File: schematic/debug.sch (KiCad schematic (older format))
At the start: 20 parts, among them J301 DEBUG HEADER, J302 DEBUG HEADER, U301 ATF16V8C_DEBUG, U302 ATF16V8C_DEBUG

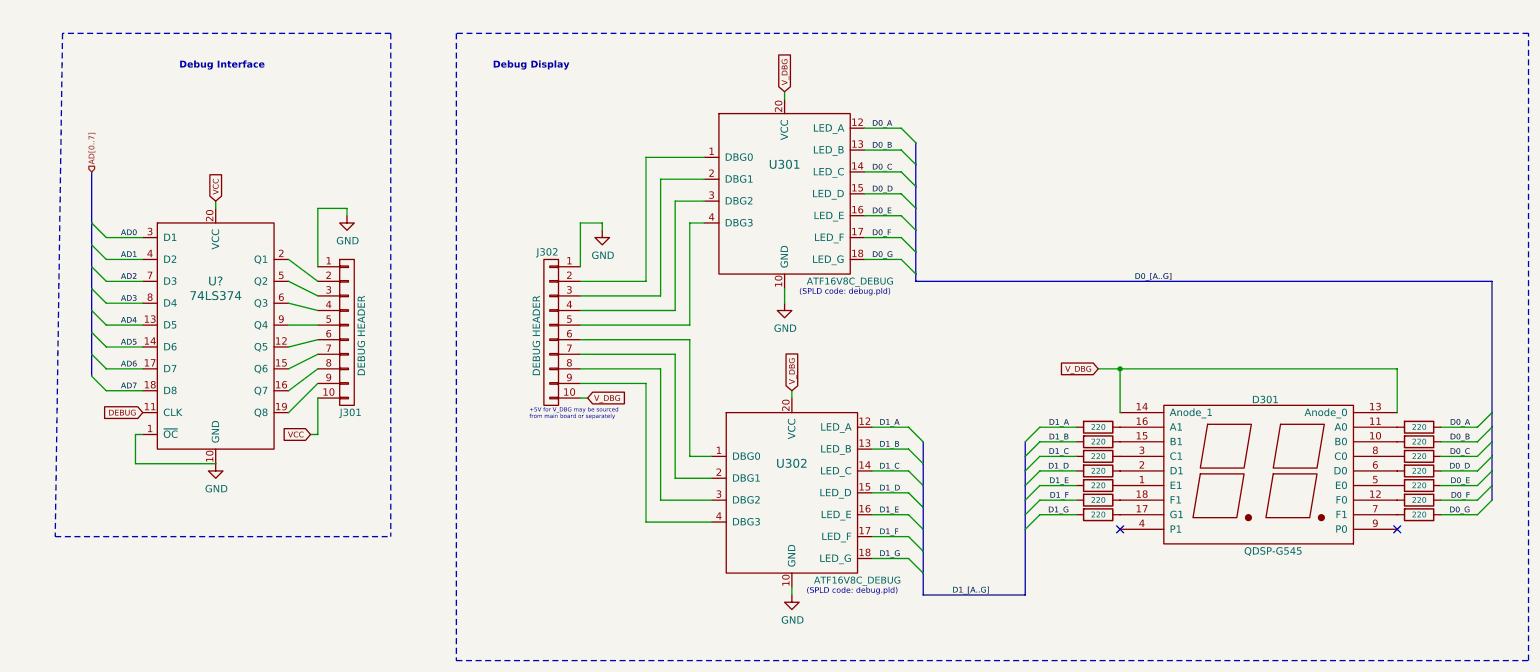
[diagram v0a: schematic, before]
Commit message: [L3] Update schematic with new NVRAM signals
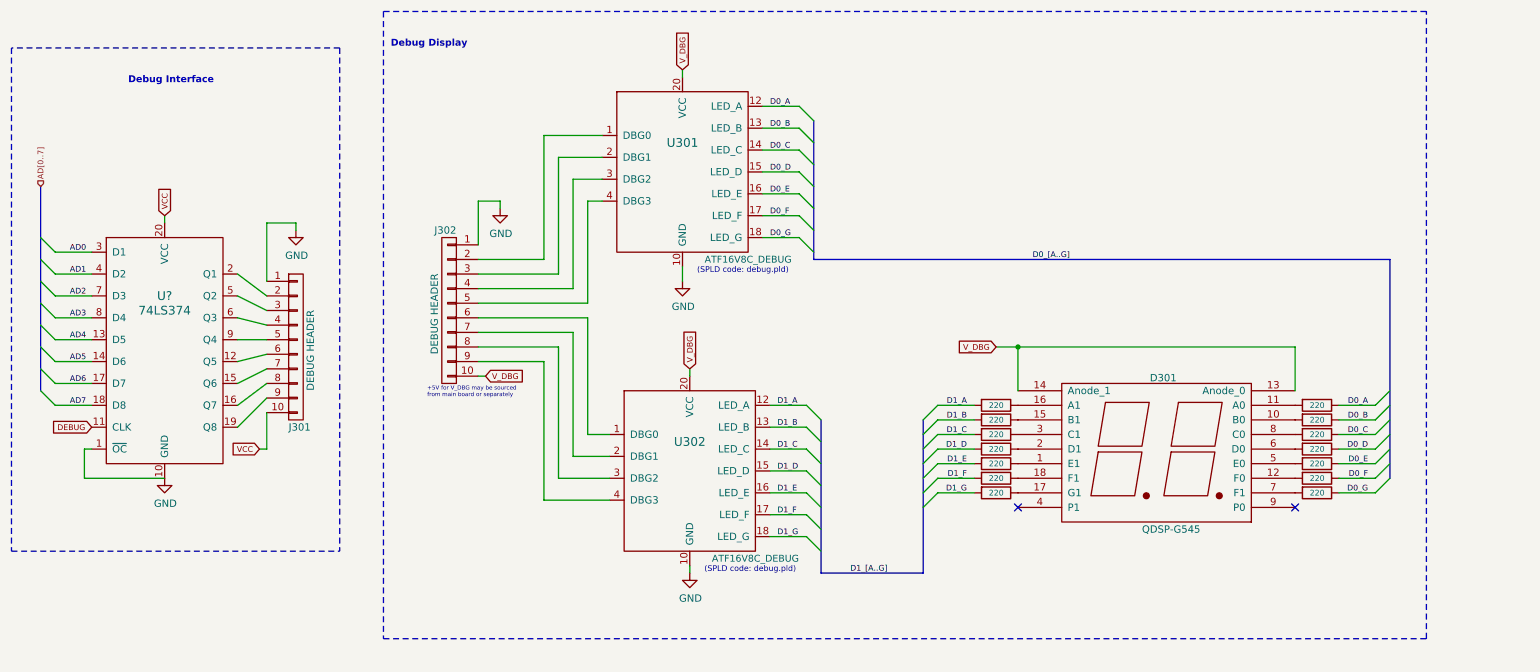
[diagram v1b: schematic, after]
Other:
- moved on the sheet: D301, J301, J302, U301, U302, U?
